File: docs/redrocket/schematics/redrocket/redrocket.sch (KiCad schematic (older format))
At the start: 6 parts

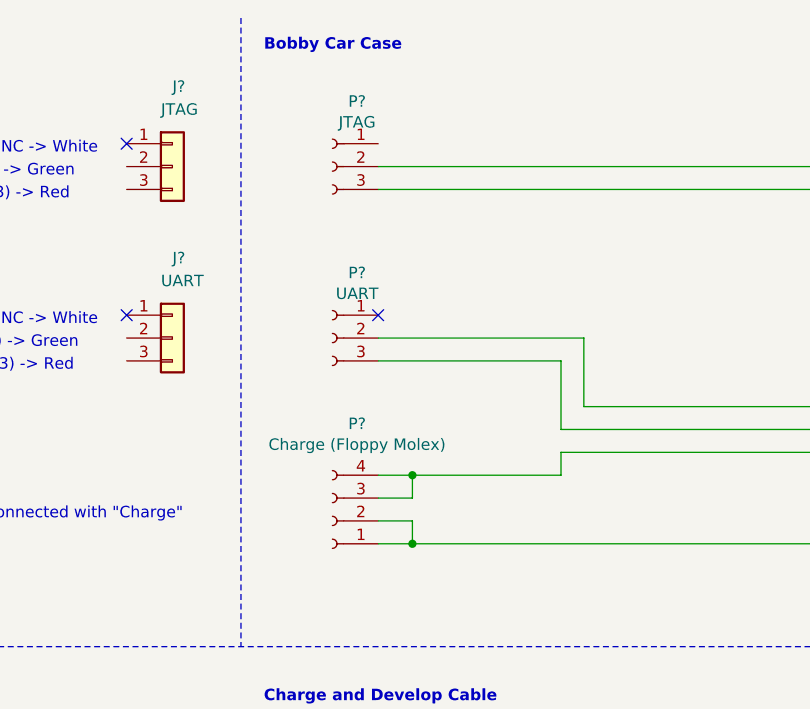
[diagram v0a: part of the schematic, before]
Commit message: Redrocket schematics: Add cable indications
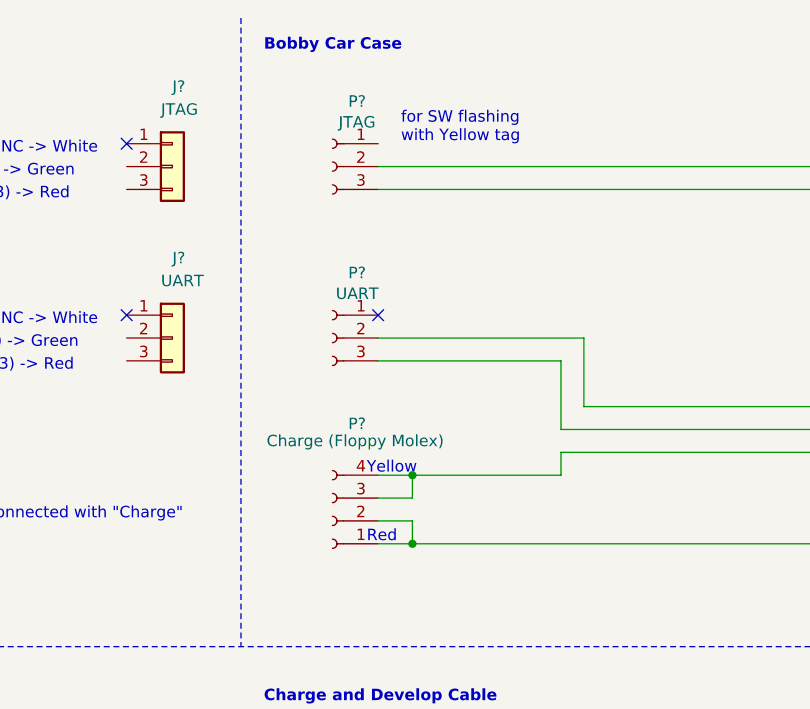
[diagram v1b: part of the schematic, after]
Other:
- note added: "Red"
- note added: "Yellow"
- note added: "for SW flashing\nwith Yellow tag"
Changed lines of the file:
@@
 P 4650 2700
 F 0 "P?" H 4542 2275 50  0000 C CNN
-F 1 "Charge (Floppy Molex)" H 4542 2366 50  0000 C CNN
+F 1 "Charge (Floppy Molex)" H 4550 2350 50  0000 C CNN
 F 2 "" H 4650 2700 50  0001 C CNN
 F 3 "~" H 4650 2700 50  0001 C CNN
@@
 Text Notes 4750 3650 0    50   ~ 0
 TODO
+Text Notes 4800 2800 0    50   ~ 0
+Red
+Text Notes 4800 2500 0    50   ~ 0
+Yellow
+Text Notes 4950 1050 0    50   ~ 0
+for SW flashing\nwith Yellow tag
 $EndSCHEMATC

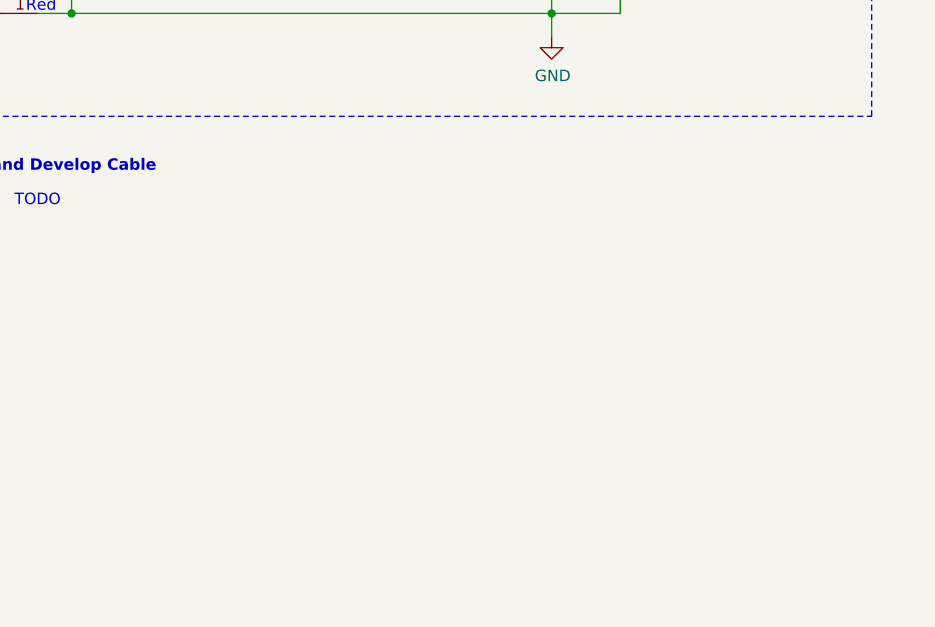
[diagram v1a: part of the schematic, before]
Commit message: Redrocket: Add schematics for Charge and Dev Cable
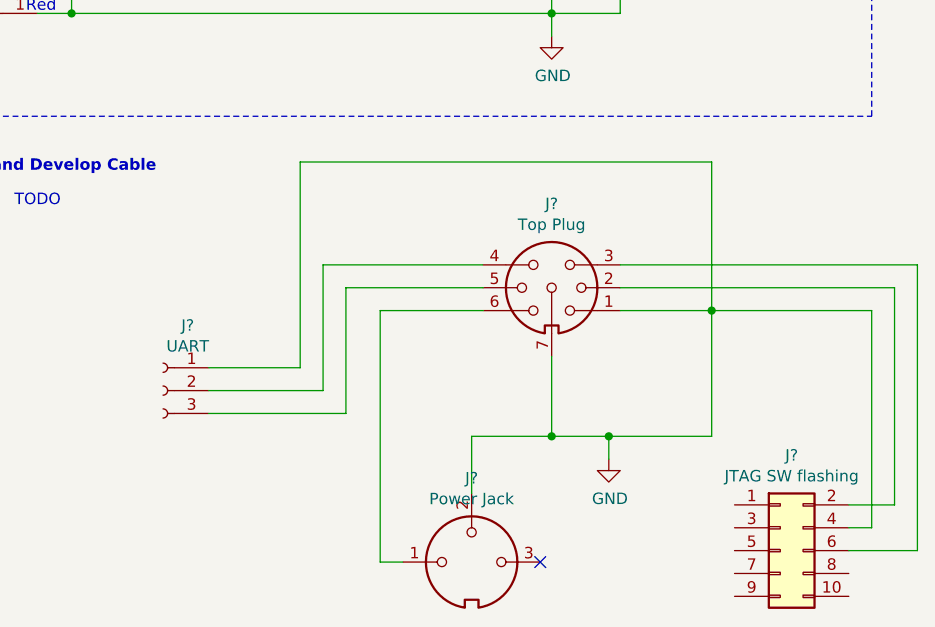
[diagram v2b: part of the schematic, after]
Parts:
- added J?: Power Jack, symbol Connector:DIN-3
- added J?: Top Plug, symbol Connector:DIN-7_CenterPin7
- added J?: JTAG SW flashing, symbol Connector_Generic:Conn_02x05_Odd_Even
- added J?: UART, symbol Connector:Conn_01x03_Female
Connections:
- net GND: now also J?.1, J?.1 (Pin_1), J?.2, J?.4 (Pin_4), J?.7
- new net: J?.1, J?.6
- new net: J?.2, J?.2 (Pin_2)
- new net: J?.3, J?.6 (Pin_6)
- new net: J?.2 (Pin_2), J?.4
- new net: J?.3 (Pin_3), J?.5
- no-connect marks 3 -> 4
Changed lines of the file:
@@
 Text Notes 4950 1050 0    50   ~ 0
 for SW flashing\nwith Yellow tag
+$Comp
+L Connector:DIN-3 J?
+U 1 1 6089DB8A
+P 6750 5200
+F 0 "J?" H 6750 5567 50  0000 C CNN
+F 1 "Power Jack" H 6750 5476 50  0000 C CNN
+F 2 "" H 6750 5200 50  0001 C CNN
+F 3 "http://www.mouser.com/ds/2/18/40_c091_abd_e-75918.pdf" H 6750 5200 50  0001 C CNN
+	1    6750 5200
+	1    0    0    -1
+$EndComp
+$Comp
+L Connector:DIN-7_CenterPin7 J?
+U 1 1 6089E6F1
+P 7100 4000
+F 0 "J?" H 7100 4367 50  0000 C CNN
+F 1 "Top Plug" H 7100 4276 50  0000 C CNN
+F 2 "" H 7100 4000 50  0001 C CNN
+F 3 "http://www.mouser.com/ds/2/18/40_c091_abd_e-75918.pdf" H 7100 4000 50  0001 C CNN
+	1    7100 4000
+	1    0    0    -1
+$EndComp
+$Comp
+L Connector_Generic:Conn_02x05_Odd_Even J?
+U 1 1 608AD799
+P 8100 5150
+F 0 "J?" H 8150 5567 50  0000 C CNN
+F 1 "JTAG SW flashing" H 8150 5476 50  0000 C CNN
+F 2 "" H 8100 5150 50  0001 C CNN
+F 3 "~" H 8100 5150 50  0001 C CNN
+	1    8100 5150
+	1    0    0    -1
+$EndComp
+$Comp
+L Connector:Conn_01x03_Female J?
+U 1 1 608AE612
+P 5400 4450
+F 0 "J?" H 5292 4735 50  0000 C CNN
+F 1 "UART" H 5292 4644 50  0000 C CNN
+F 2 "" H 5400 4450 50  0001 C CNN
+F 3 "~" H 5400 4450 50  0001 C CNN
+	1    5400 4450
+	-1   0    0    -1
+$EndComp
+Wire Wire Line
+	7100 4300 7100 4650
+Wire Wire Line
+	7100 4650 6750 4650
+Wire Wire Line
+	6750 4650 6750 4900
+Wire Wire Line
+	6350 4100 6350 5200
+Wire Wire Line
+	6350 5200 6450 5200
+Wire Wire Line
+	6350 4100 6800 4100
+NoConn ~ 7050 5200
+Wire Wire Line
+	7400 4100 7800 4100
+Wire Wire Line
+	7800 4100 7800 3450
+Wire Wire Line
+	7800 3450 6000 3450
+Wire Wire Line
+	6000 3450 6000 4350
+Wire Wire Line
+	6000 4350 5600 4350
+Wire Wire Line
+	5600 4550 6200 4550
+Wire Wire Line
+	6200 4550 6200 4000
+Wire Wire Line
+	6200 4000 6800 4000
+Wire Wire Line
+	6800 3900 6100 3900
+Wire Wire Line
+	6100 3900 6100 4450
+Wire Wire Line
+	6100 4450 5600 4450
+Wire Wire Line
+	8400 4950 8600 4950
+Wire Wire Line
+	8600 4950 8600 4000
+Wire Wire Line
+	8600 4000 7400 4000
+Wire Wire Line
+	8400 5150 8700 5150
+Wire Wire Line
+	8700 5150 8700 3900
+Wire Wire Line
+	8700 3900 7400 3900
+Wire Wire Line
+	8400 5050 8500 5050
+Wire Wire Line
+	8500 5050 8500 4100
+Wire Wire Line
+	8500 4100 7800 4100
+Connection ~ 7800 4100
+Wire Wire Line
+	7100 4650 7350 4650
+Wire Wire Line
+	7800 4650 7800 4100
+Connection ~ 7100 4650
+$Comp
+L power:GND #PWR?
+U 1 1 608E744E
+P 7350 4750
+F 0 "#PWR?" H 7350 4500 50  0001 C CNN
+F 1 "GND" H 7355 4577 50  0000 C CNN
+F 2 "" H 7350 4750 50  0001 C CNN
+F 3 "" H 7350 4750 50  0001 C CNN
+	1    7350 4750
+	1    0    0    -1
+$EndComp
+Wire Wire Line
+	7350 4750 7350 4650
+Connection ~ 7350 4650
+Wire Wire Line
+	7350 4650 7800 4650
 $EndSCHEMATC

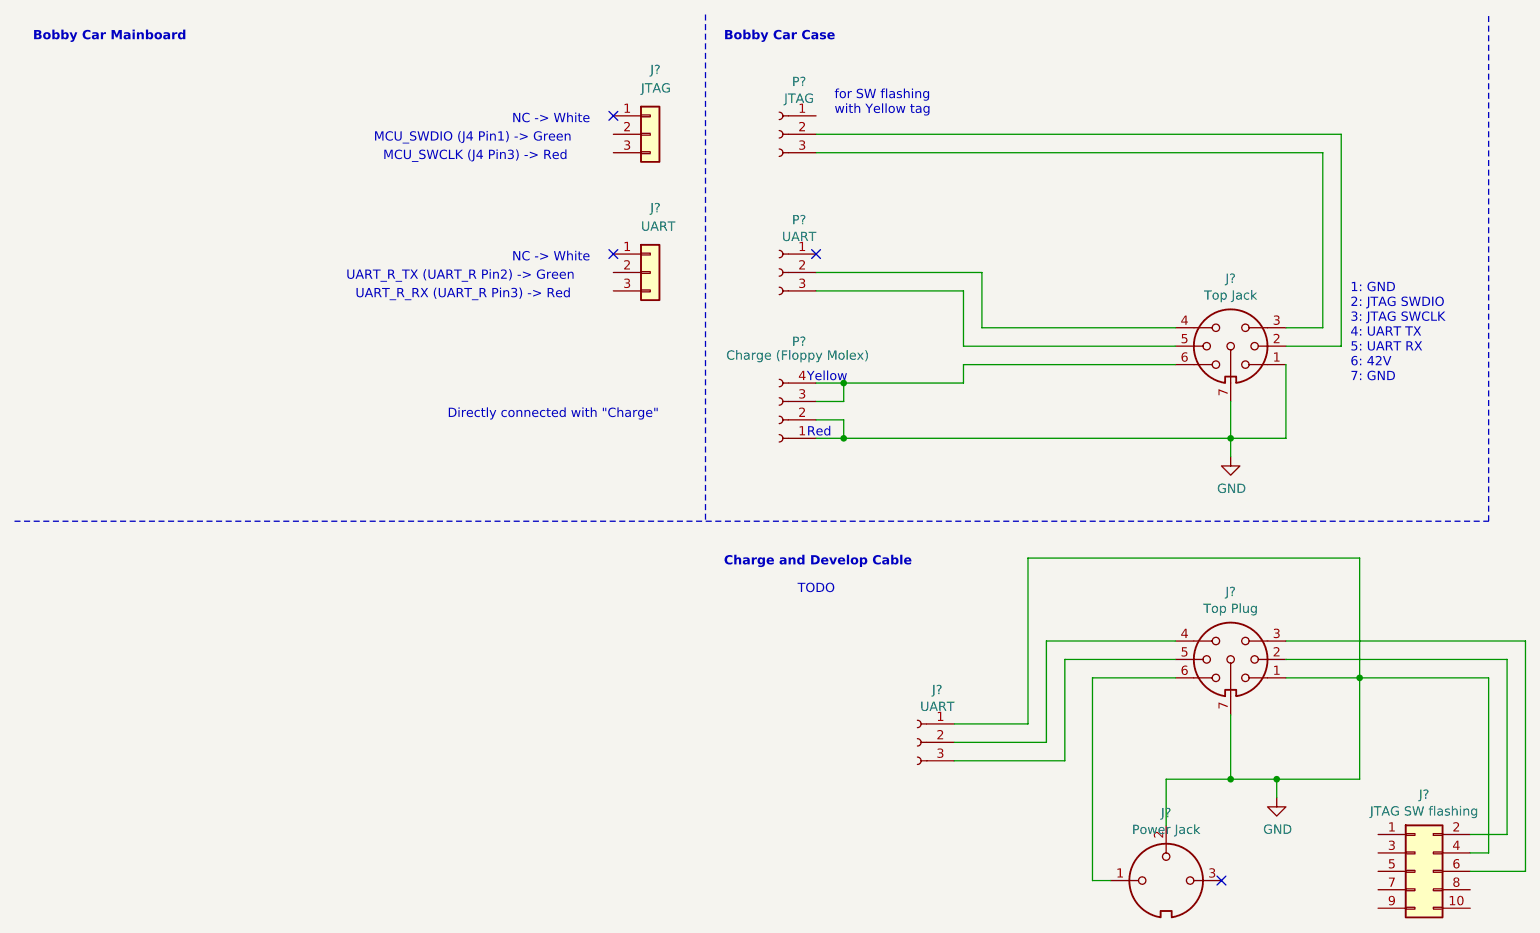
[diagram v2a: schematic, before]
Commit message: Redrocket: Fix JTAG/UART GND
needs to be disconnected from "big" battery GND, otherwise cable was not
working. Maybe too much capacity? Dunno
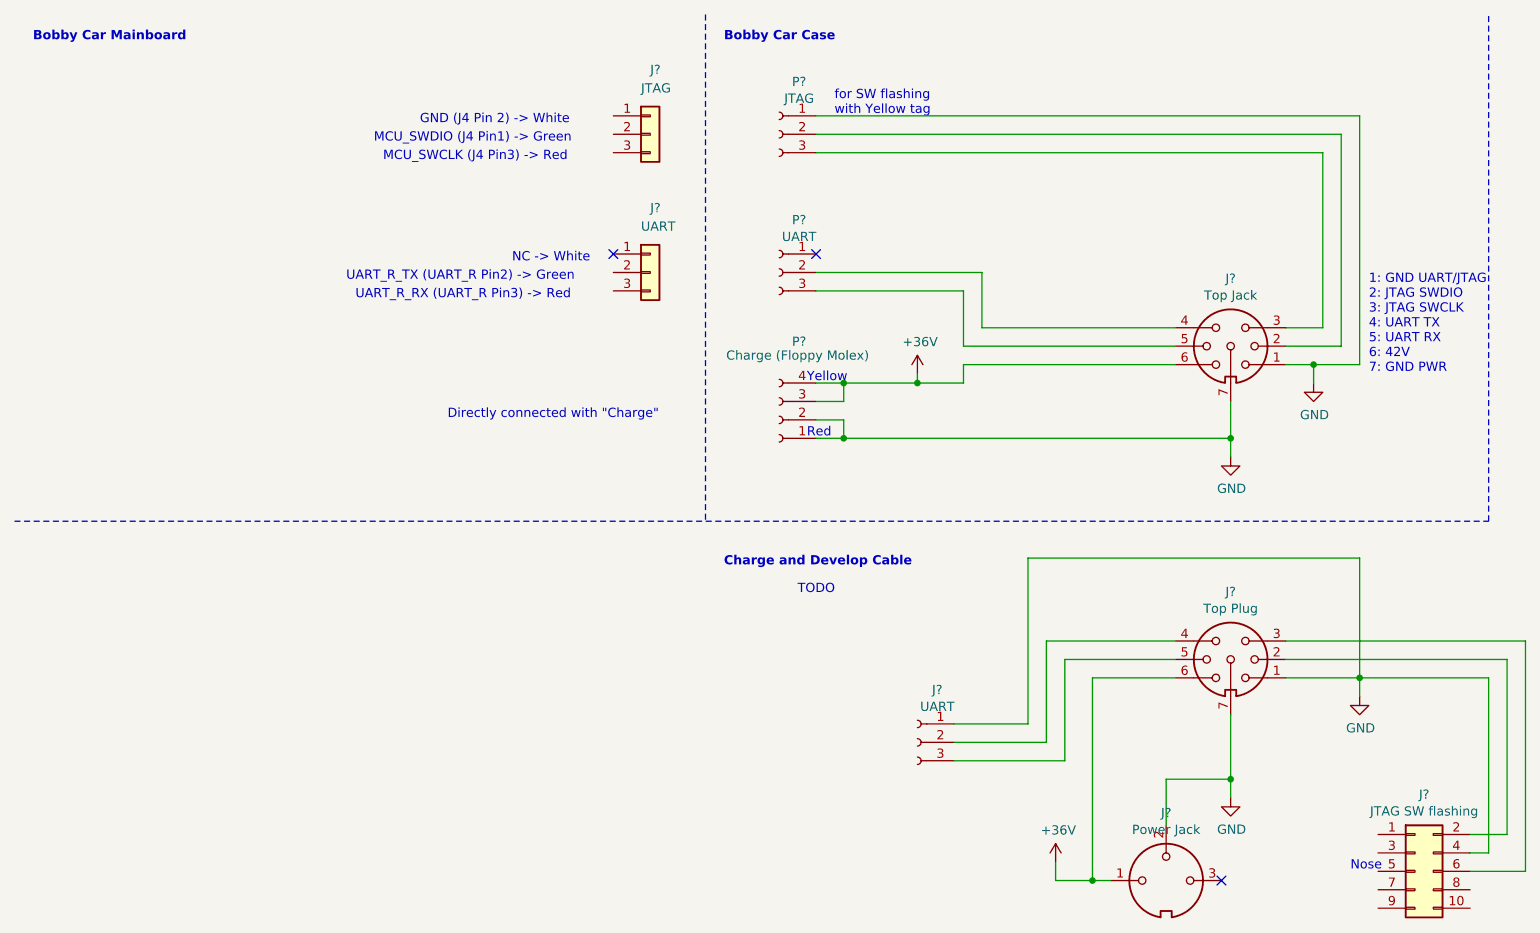
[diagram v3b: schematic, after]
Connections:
- net GND: now also P?.1 (Pin_1)
- net +36V: now reaches J?.6, P?.3 (Pin_3), P?.4 (Pin_4)
- net +36V: now also J?.1, J?.6
- no-connect marks 4 -> 3
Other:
- note added: "1: GND UART/JTAG\n2: JTAG SWDIO\n3: JTAG SWCLK\n4: UART TX\n5: UART RX\n6: 42V\n7: GND PWR"
- note added: "GND (J4 Pin 2) -> White"
- note added: "Nose"
- note removed: "1: GND\n2: JTAG SWDIO\n3: JTAG SWCLK\n4: UART TX\n5: UART RX\n6: 42V\n7: GND"
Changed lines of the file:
@@
 Wire Wire Line
 	4850 1900 5750 1900
-NoConn ~ 3750 1050
-Text Notes 3200 1100 0    50   ~ 0
-NC -> White
+Text Notes 2700 1100 0    50   ~ 0
+GND (J4 Pin 2) -> White
 Wire Wire Line
 	4850 1250 7600 1250
@@
 	7100 2600 7100 2800
 Wire Wire Line
-	7400 2400 7400 2800
-Wire Wire Line
-	7400 2800 7100 2800
-Wire Wire Line
 	4850 2500 5000 2500
 Wire Wire Line
 	5000 2500 5000 2600
-Wire Wire Line
-	5000 2500 5650 2500
 Wire Wire Line
 	5650 2500 5650 2400
@@
 Text Notes 2450 1200 0    50   ~ 0
 MCU_SWDIO (J4 Pin1) -> Green
-Text Notes 7750 2500 0    50   ~ 0
-1: GND\n2: JTAG SWDIO\n3: JTAG SWCLK\n4: UART TX\n5: UART RX\n6: 42V\n7: GND
+Text Notes 7850 2450 0    50   ~ 0
+1: GND UART/JTAG\n2: JTAG SWDIO\n3: JTAG SWCLK\n4: UART TX\n5: UART RX\n6: 42V\n7: GND PWR
 Text Notes 2850 2700 0    50   ~ 0
 Directly connected with "Charge"
@@
 	8500 4100 7800 4100
 Connection ~ 7800 4100
-Wire Wire Line
-	7100 4650 7350 4650
-Wire Wire Line
-	7800 4650 7800 4100
 Connection ~ 7100 4650
 $Comp
 L power:GND #PWR?
 U 1 1 608E744E
-P 7350 4750
-F 0 "#PWR?" H 7350 4500 50  0001 C CNN
-F 1 "GND" H 7355 4577 50  0000 C CNN
-F 2 "" H 7350 4750 50  0001 C CNN
-F 3 "" H 7350 4750 50  0001 C CNN
-	1    7350 4750
-	1    0    0    -1
-$EndComp
-Wire Wire Line
-	7350 4750 7350 4650
-Connection ~ 7350 4650
-Wire Wire Line
-	7350 4650 7800 4650
+P 7100 4750
+F 0 "#PWR?" H 7100 4500 50  0001 C CNN
+F 1 "GND" H 7105 4577 50  0000 C CNN
+F 2 "" H 7100 4750 50  0001 C CNN
+F 3 "" H 7100 4750 50  0001 C CNN
+	1    7100 4750
+	1    0    0    -1
+$EndComp
+Text Notes 7750 5150 0    50   ~ 0
+Nose
+Wire Wire Line
+	7100 4750 7100 4650
+$Comp
+L power:GND #PWR?
+U 1 1 608D773D
+P 7800 4200
+F 0 "#PWR?" H 7800 3950 50  0001 C CNN
+F 1 "GND" H 7805 4027 50  0000 C CNN
+F 2 "" H 7800 4200 50  0001 C CNN
+F 3 "" H 7800 4200 50  0001 C CNN
+	1    7800 4200
+	1    0    0    -1
+$EndComp
+Wire Wire Line
+	7800 4200 7800 4100
+Wire Wire Line
+	4850 1050 7800 1050
+Wire Wire Line
+	7800 1050 7800 2400
+Wire Wire Line
+	7400 2400 7550 2400
+$Comp
+L power:GND #PWR?
+U 1 1 608DCD67
+P 7550 2500
+F 0 "#PWR?" H 7550 2250 50  0001 C CNN
+F 1 "GND" H 7555 2327 50  0000 C CNN
+F 2 "" H 7550 2500 50  0001 C CNN
+F 3 "" H 7550 2500 50  0001 C CNN
+	1    7550 2500
+	1    0    0    -1
+$EndComp
+Wire Wire Line
+	7550 2500 7550 2400
+Connection ~ 7550 2400
+Wire Wire Line
+	7550 2400 7800 2400
+$Comp
+L power:+36V #PWR?
+U 1 1 608E6F34
+P 6150 5100
+F 0 "#PWR?" H 6150 4950 50  0001 C CNN
+F 1 "+36V" H 6165 5273 50  0000 C CNN
+F 2 "" H 6150 5100 50  0001 C CNN
+F 3 "" H 6150 5100 50  0001 C CNN
+	1    6150 5100
+	1    0    0    -1
+$EndComp
+Wire Wire Line
+	6150 5200 6350 5200
+Connection ~ 6350 5200
+Wire Wire Line
+	6150 5200 6150 5100
+Wire Wire Line
+	5000 2500 5400 2500
+$Comp
+L power:+36V #PWR?
+U 1 1 608F3875
+P 5400 2450
+F 0 "#PWR?" H 5400 2300 50  0001 C CNN
+F 1 "+36V" H 5415 2623 50  0000 C CNN
+F 2 "" H 5400 2450 50  0001 C CNN
+F 3 "" H 5400 2450 50  0001 C CNN
+	1    5400 2450
+	1    0    0    -1
+$EndComp
+Wire Wire Line
+	5400 2450 5400 2500
+Connection ~ 5400 2500
+Wire Wire Line
+	5400 2500 5650 2500
 $EndSCHEMATC
